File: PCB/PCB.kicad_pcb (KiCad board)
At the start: 2 copper layers, 222.6 x 128.5 mm, 78 parts, among them SW10 SW_Push, SW11 SW_Push, SW12 SW_Push, SW13 SW_Push, SW14 SW_Push, SW15 SW_Push, SW16 SW_Push, SW17 SW_Push, SW18 SW_Push, SW19 SW_Push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

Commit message: get rid of lock files
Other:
- board size 222.6 x 128.5 mm -> 143.2 x 113.5 mm
- board text added: "Made by @itsme with skill issues"
- board text added: "STNO"

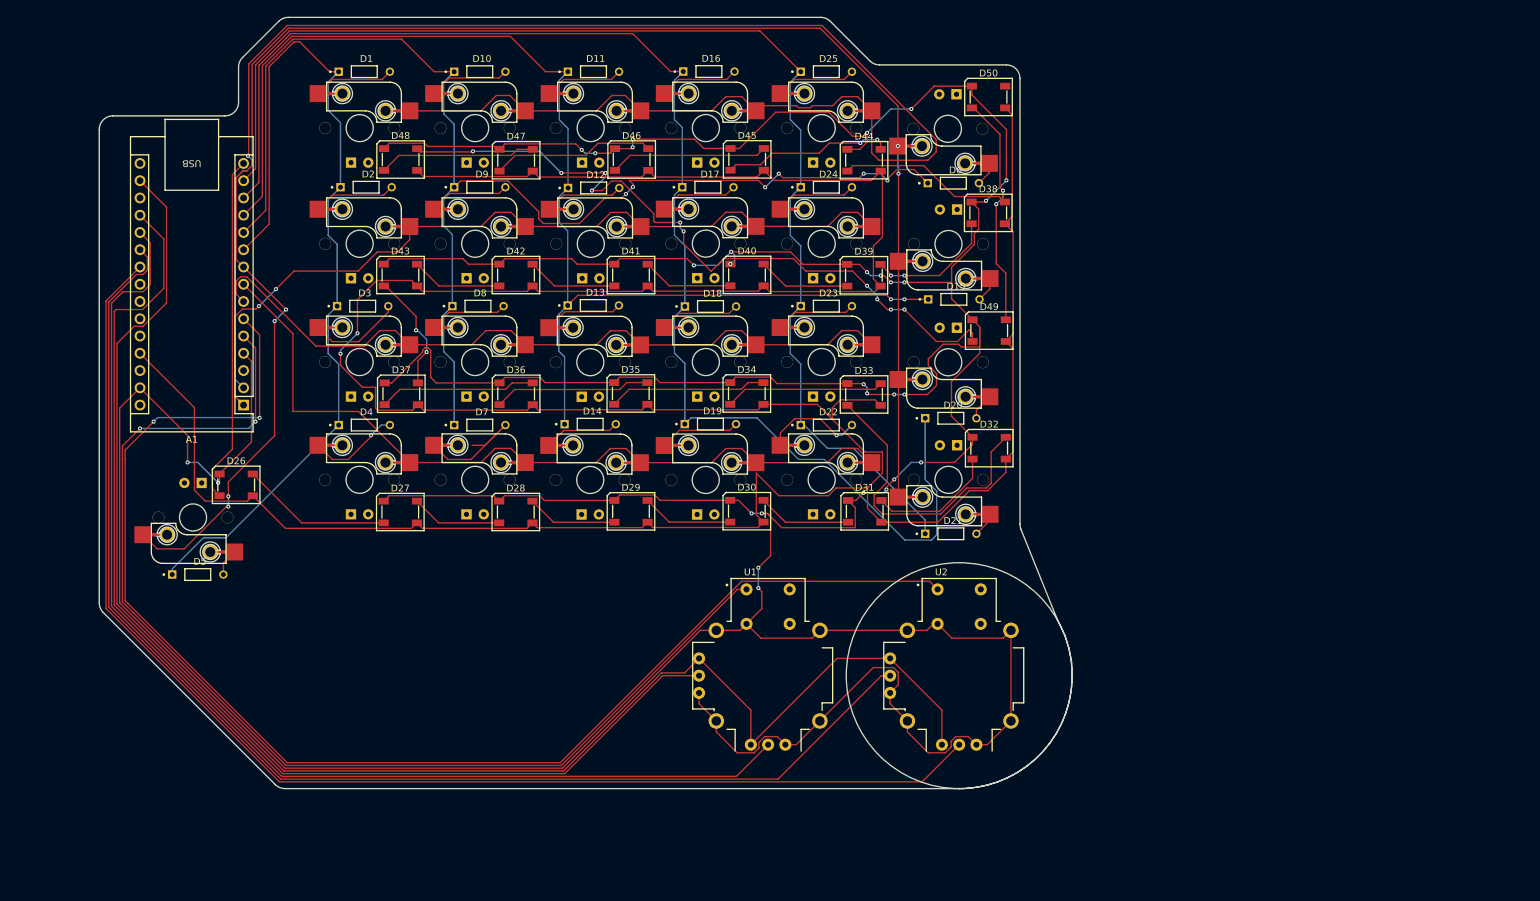
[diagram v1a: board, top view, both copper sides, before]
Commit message: move text to the right layer and fix the edge cuts
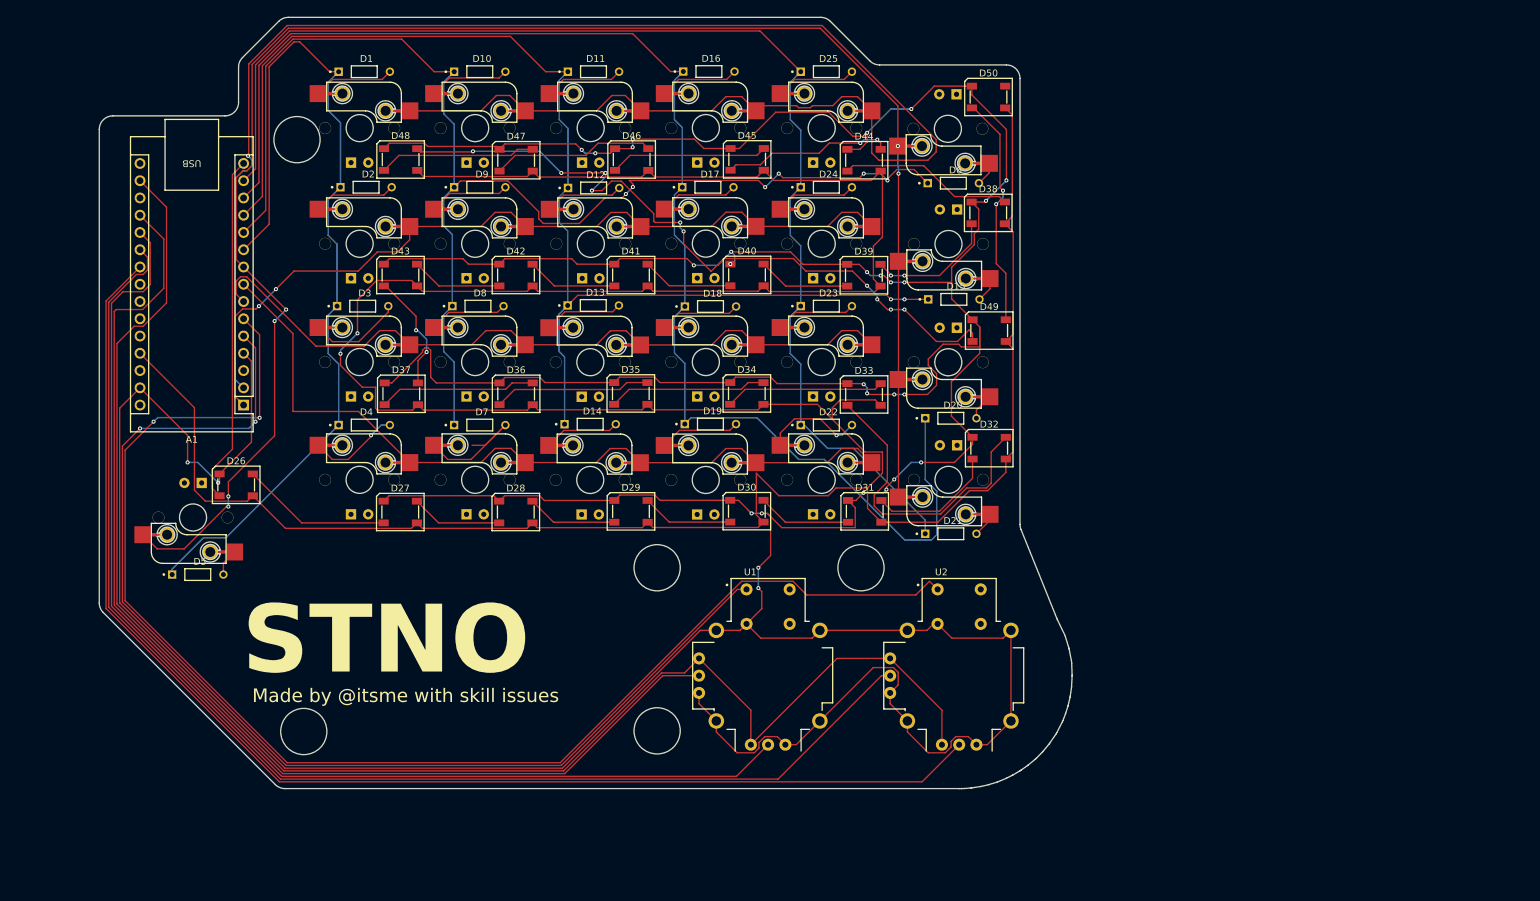
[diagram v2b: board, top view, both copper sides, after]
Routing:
- net SEL2: track 200.5 -> 202.2 mm
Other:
- outline, holes or cut-outs redrawn
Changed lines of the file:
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@@
 		(tenting front back)
 		(pcbplotparams
-			(layerselection 0x00000000_00000000_55555555_5755f5ff)
+			(layerselection 0x00000000_00000000_55555555_57555550)
 			(plot_on_all_layers_selection 0x00000000_00000000_00000000_00000000)
 			(disableapertmacros no)
@@
 			(plotframeref no)
 			(mode 1)
-			(useauxorigin no)
+			(useauxorigin yes)
 			(hpglpennumber 1)
 			(hpglpenspeed 20)
@@
 			(pdf_single_document no)
 			(dxfpolygonmode yes)
-			(dxfimperialunits yes)
+			(dxfimperialunits no)
 			(dxfusepcbnewfont yes)
 			(psnegative no)
@@
 			(crossoutdnponfab yes)
 			(subtractmaskfromsilk no)
-			(outputformat 1)
+			(outputformat 5)
 			(mirror no)
-			(drillshape 1)
+			(drillshape 0)
 			(scaleselection 1)
 			(outputdirectory "")
@@
 	)
 	(gr_line
-		(start 182.411316 143.494986)
+		(start 182.411316 143.5)
 		(end 182.745012 143.490915)
 		(stroke
@@
 		(layer "Edge.Cuts")
 	)
+	(gr_circle
+		(center 85.6 135.1)
+		(end 89 135.1)
+		(stroke
+			(width 0.05)
+			(type default)
+		)
+		(fill no)
+		(layer "Edge.Cuts")
+	)
 	(gr_arc
 		(start 195.359874 136.837326)
@@
 		(layer "Edge.Cuts")
 	)
+	(gr_circle
+		(center 137.6 111)
+		(end 141 111)
+		(stroke
+			(width 0.05)
+			(type default)
+		)
+		(fill no)
+		(layer "Edge.Cuts")
+	)
 	(gr_arc
 		(start 198.569607 124.700469)
@@
 		(layer "Edge.Cuts")
 	)
+	(gr_circle
+		(center 84.6 48)
+		(end 88 48)
+		(stroke
+			(width 0.05)
+			(type default)
+		)
+		(fill no)
+		(layer "Edge.Cuts")
+	)
 	(gr_arc
 		(start 161.671573 30)
@@
 	(gr_line
 		(start 182.053514 143.49982)
-		(end 182.408684 143.49502)
+		(end 182.408684 143.5)
 		(stroke
 			(width 0.05)
@@
 	(gr_line
 		(start 82.828427 143.5)
-		(end 182.026485 143.500003)
+		(end 182.0264 143.500003)
 		(stroke
 			(width 0.05)
@@
 		(layer "Edge.Cuts")
 	)
+	(gr_circle
+		(center 137.6 135)
+		(end 141 135)
+		(stroke
+			(width 0.05)
+			(type default)
+		)
+		(fill no)
+		(layer "Edge.Cuts")
+	)
 	(gr_line
 		(start 55.5 46.5)
@@
 	)
 	(gr_circle
-		(center 182.05 126.88)
-		(end 182.04 143.5)
+		(center 167.6 111)
+		(end 171 111)
 		(stroke
 			(width 0.05)
@@
 		(layer "Edge.Cuts")
 	)
-	(gr_text "STNO"
-		(at 78.5 126 0)
-		(layer "Edge.Cuts")
+	(gr_text "Made by @itsme with skill issues"
+		(at 78 131 0)
+		(layer "F.SilkS")
 		(effects
 			(font
-				(size 10 10)
-				(thickness 1.5)
-				(bold yes)
+				(size 2 2)
+				(thickness 0.3)
 			)
 			(justify left bottom)
 		)
 	)
-	(gr_text "Made by @itsme with skill issues"
-		(at 80 129.5 0)
-		(layer "Edge.Cuts")
+	(gr_text "STNO"
+		(at 76.5 127.5 0)
+		(layer "F.SilkS")
 		(effects
 			(font
-				(size 2 2)
-				(thickness 0.3)
+				(size 10 10)
+				(thickness 1.5)
+				(bold yes)
 			)
 			(justify left bottom)
@@
 	)
 	(segment
-		(start 123.3339 139.693)
-		(end 84.5 139.693)
+		(start 63.5 89.5)
+		(end 59.307 93.693)
 		(width 0.2)
 		(layer "F.Cu")
@@
 	(segment
 		(start 83.1627 139.693)
-		(end 59.73485 116.26515)
+		(end 123.3339 139.693)
 		(width 0.2)
 		(layer "F.Cu")
@@
 	)
 	(segment
-		(start 59.307 95)
-		(end 59.307 93.693)
+		(start 59.307 93.693)
+		(end 59.307 115.8373)
 		(width 0.2)
 		(layer "F.Cu")
@@
 	)
 	(segment
-		(start 59.73485 116.26515)
-		(end 59.307 115.8373)
+		(start 175.6753 115.001)
+		(end 177.685 112.9913)
 		(width 0.2)
 		(layer "F.Cu")
@@
 	)
 	(segment
-		(start 150.0356 112.9913)
-		(end 123.3339 139.693)
+		(start 123.3339 139.693)
+		(end 150.0356 112.9913)
 		(width 0.2)
 		(layer "F.Cu")
@@
 	)
 	(segment
-		(start 59.307 93.693)
-		(end 63.5 89.5)
+		(start 159.608015 115.001)
+		(end 175.6753 115.001)
 		(width 0.2)
 		(layer "F.Cu")
@@
 	)
 	(segment
-		(start 178.875 114.1813)
-		(end 177.685 112.9913)
+		(start 150.0356 112.9913)
+		(end 157.598315 112.9913)
 		(width 0.2)
 		(layer "F.Cu")
@@
 	)
 	(segment
-		(start 59.307 115.8373)
-		(end 59.307 95)
+		(start 157.598315 112.9913)
+		(end 159.608015 115.001)
 		(width 0.2)
 		(layer "F.Cu")
@@
 	)
 	(segment
-		(start 177.685 112.9913)
-		(end 150.0356 112.9913)
+		(start 59.307 115.8373)
+		(end 83.1627 139.693)
 		(width 0.2)
 		(layer "F.Cu")
@@
 	)
 	(segment
-		(start 84.5 139.693)
-		(end 83.1627 139.693)
+		(start 79.1 76.72)
+		(end 76.74 74.36)
 		(width 0.2)
 		(layer "F.Cu")
@@
 	)
 	(segment
-		(start 79.1 76.72)
-		(end 76.74 74.36)
+		(start 177.685 112.9913)
+		(end 178.875 114.1813)
 		(width 0.2)
 		(layer "F.Cu")
